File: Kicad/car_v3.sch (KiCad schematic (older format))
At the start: 0 parts

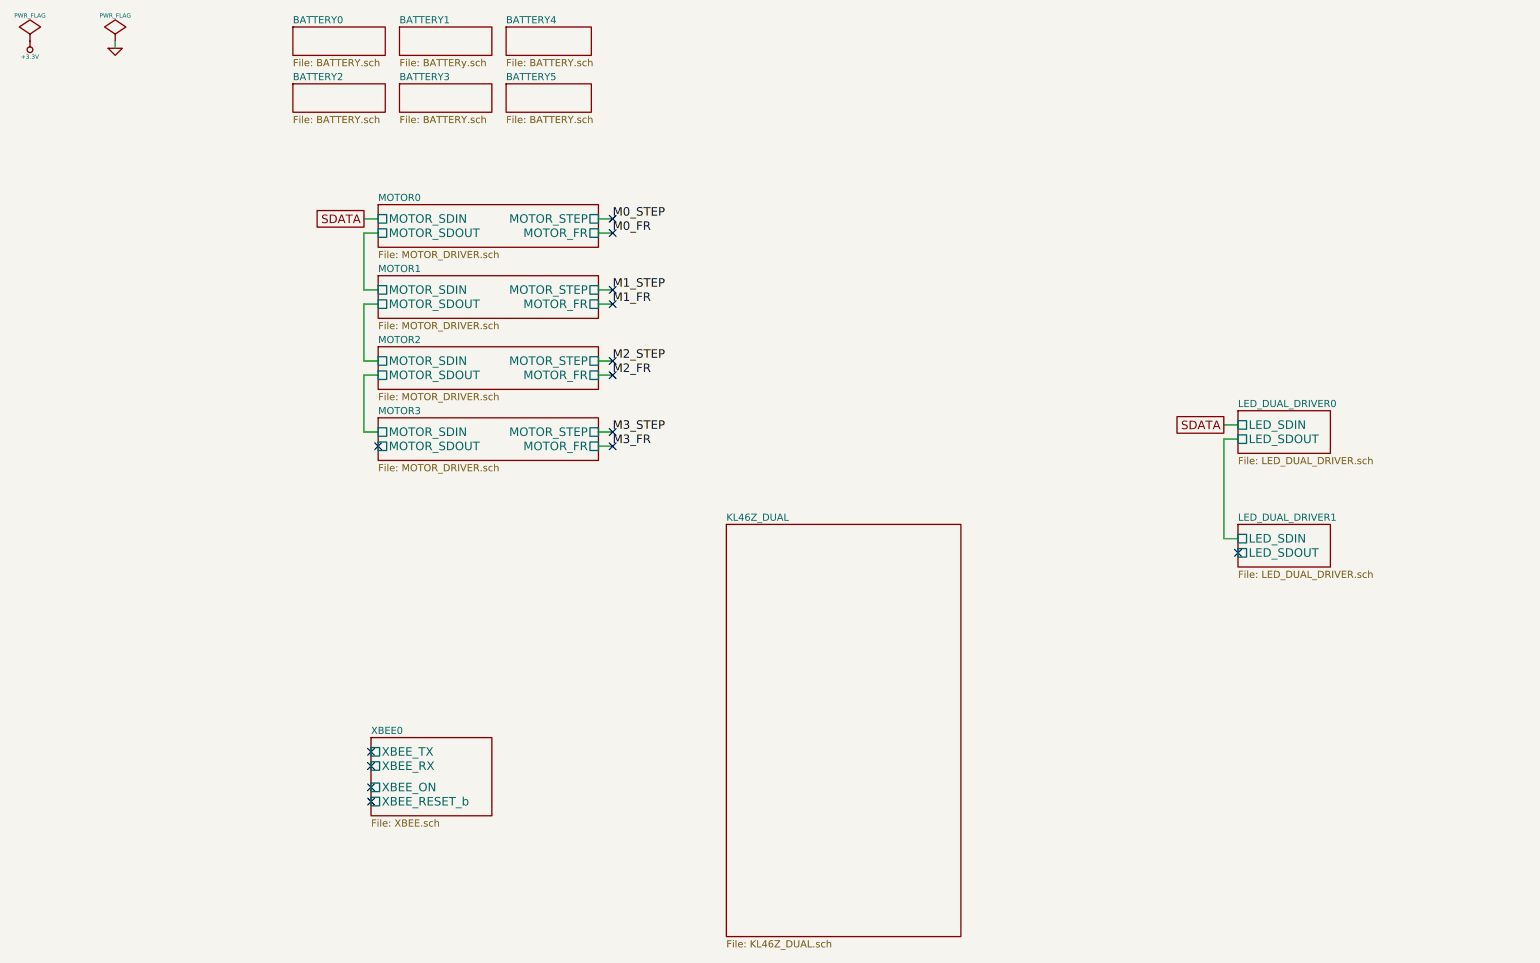
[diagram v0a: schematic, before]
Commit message: 
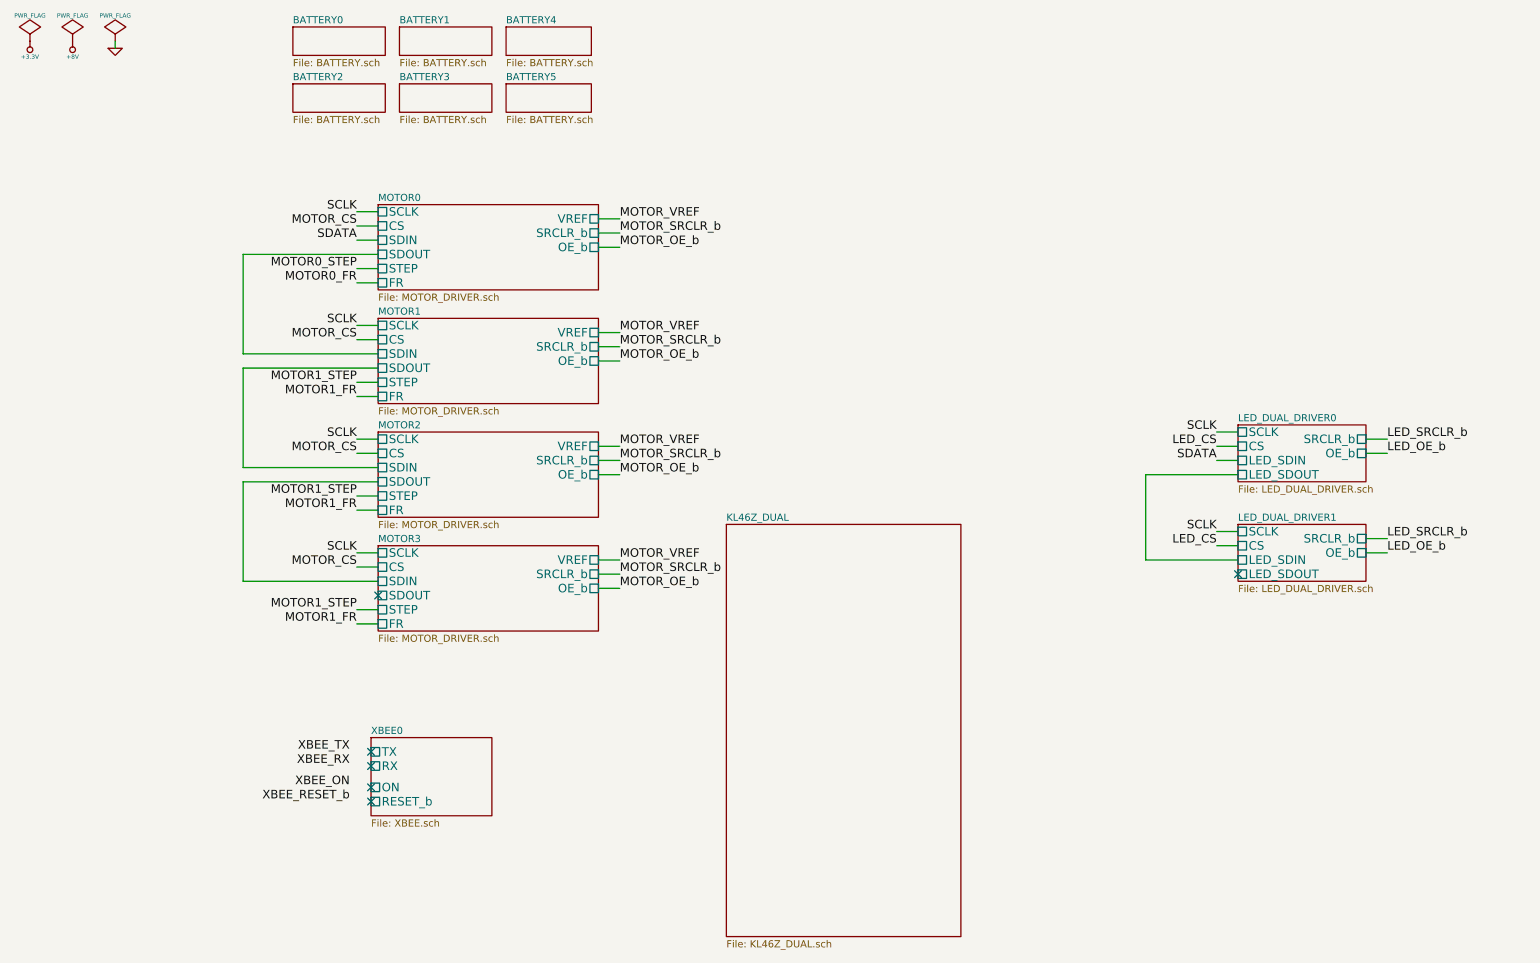
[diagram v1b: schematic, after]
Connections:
- no-connect marks 14 -> 6

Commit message: All wired. ERC passes with no errors. Might be good to go.
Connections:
- no-connect marks 6 -> 2

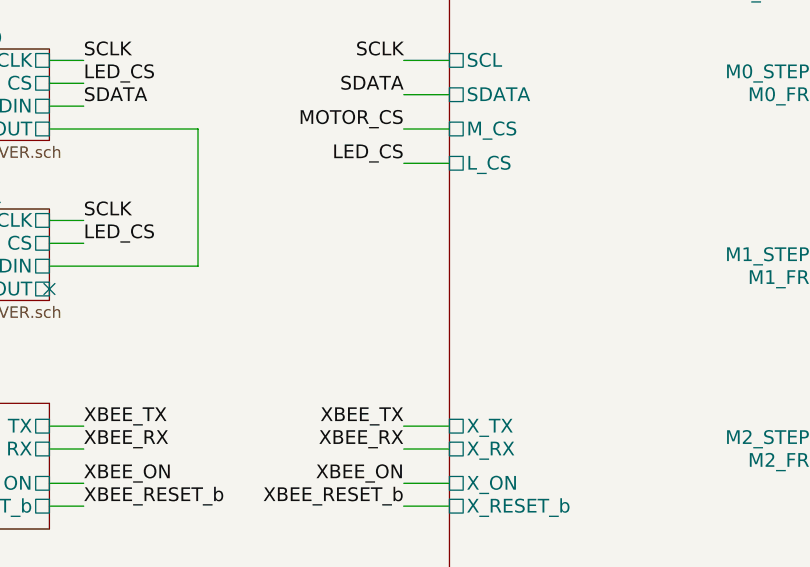
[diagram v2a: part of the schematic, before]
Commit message: 
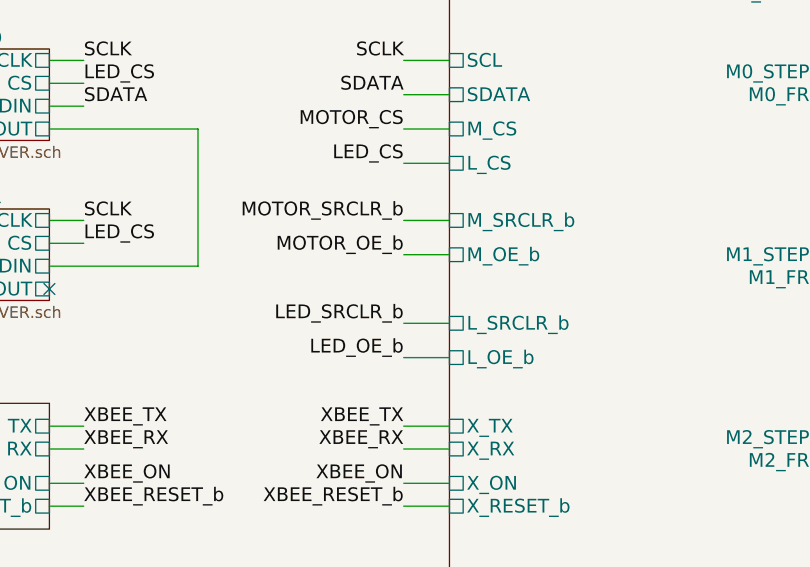
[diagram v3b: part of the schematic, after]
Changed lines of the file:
@@
 F17 "X_RESET_b" U L 4650 4250 60
 F18 "M_VREF" U R 6300 2000 60
+F19 "M_SRCLR_b" U L 4650 3000 60
+F20 "M_OE_b" U L 4650 3150 60
+F21 "L_SRCLR_b" U L 4650 3450 60
+F22 "L_OE_b" U L 4650 3600 60
 $EndSheet
 $Comp
@@
 Wire Wire Line
 	6500 2000 6300 2000
+Text Label 4450 3000 2    60   ~ 0
+MOTOR_SRCLR_b
+Text Label 4450 3150 2    60   ~ 0
+MOTOR_OE_b
+Text Label 4450 3450 2    60   ~ 0
+LED_SRCLR_b
+Text Label 4450 3600 2    60   ~ 0
+LED_OE_b
+Wire Wire Line
+	4650 3000 4450 3000
+Wire Wire Line
+	4450 3150 4650 3150
+Wire Wire Line
+	4450 3450 4650 3450
+Wire Wire Line
+	4450 3600 4650 3600
 $EndSCHEMATC

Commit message: added lines for m_srclr_b, l_srclr_b, and m_oe_b and l_oe_b. woooot.
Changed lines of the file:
@@
 	2900 2600 3550 2600
-Wire Wire Line
-	700  2600 700  3200
 Wire Wire Line
 	3550 3200 2900 3200

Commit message: 
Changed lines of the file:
@@
 LIBS:contrib
 LIBS:valves
-LIBS:___power_diode
-LIBS:__batterybarlug
-LIBS:__freedom_x
-LIBS:__xbee-pro
-LIBS:CAR
 LIBS:car_v3-cache
 EELAYER 27 0
@@
 Sheet 1 15
 Title ""
-Date "8 jun 2014"
+Date "13 jul 2014"
 Rev ""
 Comp ""
@@
 $EndSheet
 $Sheet
-S 2000 2950 900  400
+S 1800 3000 900  400
 U 5387F9D3
 F0 "LED_DUAL_DRIVER1" 50
 F1 "LED_DUAL_DRIVER.sch" 50
-F2 "SDOUT" U R 2900 3300 60
-F3 "SDIN" U R 2900 3200 60
-F4 "SCLK" U R 2900 3000 60
-F5 "CS" U R 2900 3100 60
-F6 "SRCLR_b" U L 2000 3050 60
-F7 "OE_b" U L 2000 3150 60
+F2 "SDOUT" U R 2700 3350 60
+F3 "SDIN" U R 2700 3250 60
+F4 "SCLK" U R 2700 3050 60
+F5 "CS" U R 2700 3150 60
+F6 "SRCLR_b" U L 1800 3100 60
+F7 "OE_b" U L 1800 3200 60
 $EndSheet
 $Sheet
@@
 $EndSheet
 $Sheet
-S 2000 2250 900  400
+S 1800 2300 900  400
 U 539441D7
 F0 "LED_DUAL_DRIVER0" 50
 F1 "LED_DUAL_DRIVER.sch" 50
-F2 "SDOUT" U R 2900 2600 60
-F3 "SDIN" U R 2900 2500 60
-F4 "SCLK" U R 2900 2300 60
-F5 "CS" U R 2900 2400 60
-F6 "SRCLR_b" U L 2000 2350 60
-F7 "OE_b" U L 2000 2450 60
-$EndSheet
-Text Label 3050 2300 0    60   ~ 0
-SCLK
-Text Label 3050 2500 0    60   ~ 0
+F2 "SDOUT" U R 2700 2650 60
+F3 "SDIN" U R 2700 2550 60
+F4 "SCLK" U R 2700 2350 60
+F5 "CS" U R 2700 2450 60
+F6 "SRCLR_b" U L 1800 2400 60
+F7 "OE_b" U L 1800 2500 60
+$EndSheet
+Text Label 2850 2350 0    60   ~ 0
+SCLK
+Text Label 2850 2550 0    60   ~ 0
 SDATA
-Text Label 3050 3000 0    60   ~ 0
-SCLK
-Text Label 3050 2400 0    60   ~ 0
+Text Label 2850 3050 0    60   ~ 0
+SCLK
+Text Label 2850 2450 0    60   ~ 0
 LED_CS
-Text Label 3050 3100 0    60   ~ 0
+Text Label 2850 3150 0    60   ~ 0
 LED_CS
-NoConn ~ 2900 3300
-Text Label 1850 2350 2    60   ~ 0
+NoConn ~ 2700 3350
+Text Label 1650 2400 2    60   ~ 0
 LED_SRCLR_b
-Text Label 1850 2450 2    60   ~ 0
+Text Label 1650 2500 2    60   ~ 0
 LED_OE_b
-Text Label 1850 3050 2    60   ~ 0
+Text Label 1650 3100 2    60   ~ 0
 LED_SRCLR_b
-Text Label 1850 3150 2    60   ~ 0
+Text Label 1650 3200 2    60   ~ 0
 LED_OE_b
 Text Label 3050 3900 0    60   ~ 0
@@
 	7650 3850 7650 4550
 Wire Wire Line
-	2900 2600 3550 2600
-Wire Wire Line
-	3550 3200 2900 3200
-Wire Wire Line
-	3050 3000 2900 3000
-Wire Wire Line
-	3050 3100 2900 3100
-Wire Wire Line
-	3050 2300 2900 2300
-Wire Wire Line
-	3050 2400 2900 2400
-Wire Wire Line
-	3050 2500 2900 2500
-Wire Wire Line
-	2000 2350 1850 2350
-Wire Wire Line
-	2000 2450 1850 2450
-Wire Wire Line
-	2000 3050 1850 3050
-Wire Wire Line
-	2000 3150 1850 3150
+	2700 2650 3350 2650
+Wire Wire Line
+	3350 3250 2700 3250
+Wire Wire Line
+	2850 3050 2700 3050
+Wire Wire Line
+	2850 3150 2700 3150
+Wire Wire Line
+	2850 2350 2700 2350
+Wire Wire Line
+	2850 2450 2700 2450
+Wire Wire Line
+	2850 2550 2700 2550
+Wire Wire Line
+	1800 2400 1650 2400
+Wire Wire Line
+	1800 2500 1650 2500
+Wire Wire Line
+	1800 3100 1650 3100
+Wire Wire Line
+	1800 3200 1650 3200
 Wire Wire Line
 	6500 2350 6300 2350
@@
 	6300 4850 6500 4850
 Wire Wire Line
-	3550 2600 3550 3200
+	3350 2650 3350 3250
 Wire Wire Line
 	4650 2300 4450 2300
